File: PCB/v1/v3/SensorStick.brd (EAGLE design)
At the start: 58.4 x 38.1 mm, 57 parts, among them U1 TPD4F003DQDR, Y1 ECS-TXO-3225MV-400-TR

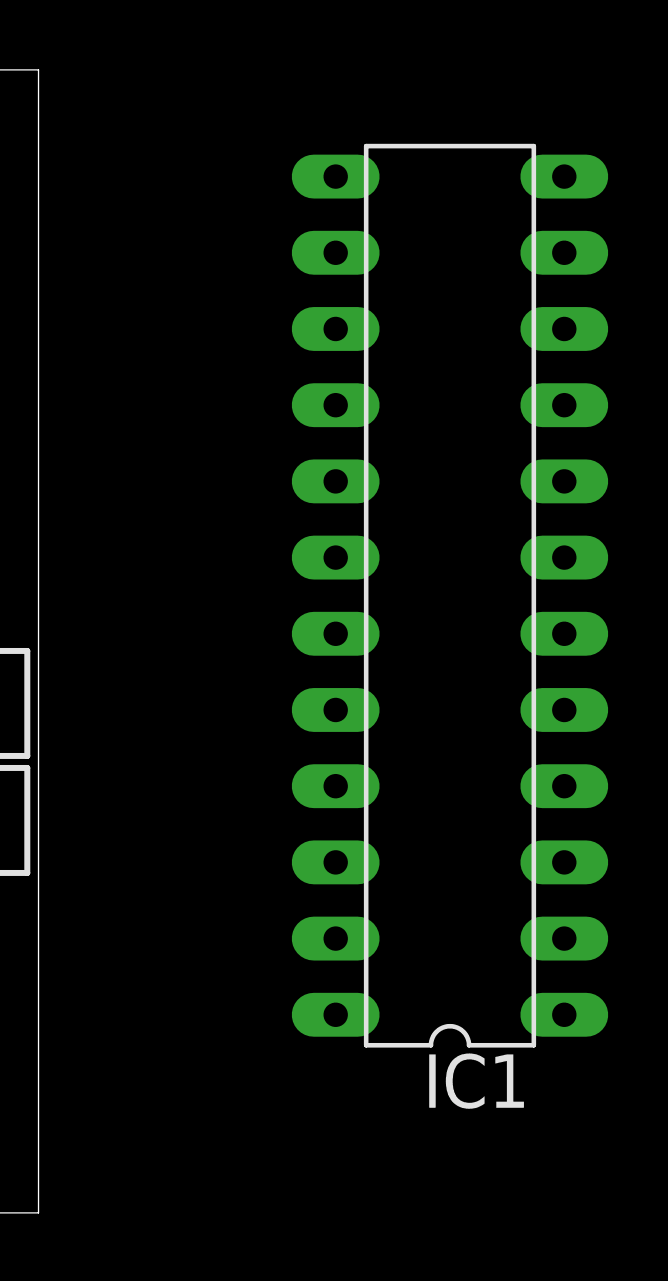
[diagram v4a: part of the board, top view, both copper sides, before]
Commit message: Jesus - Removed DIL24 IC connector
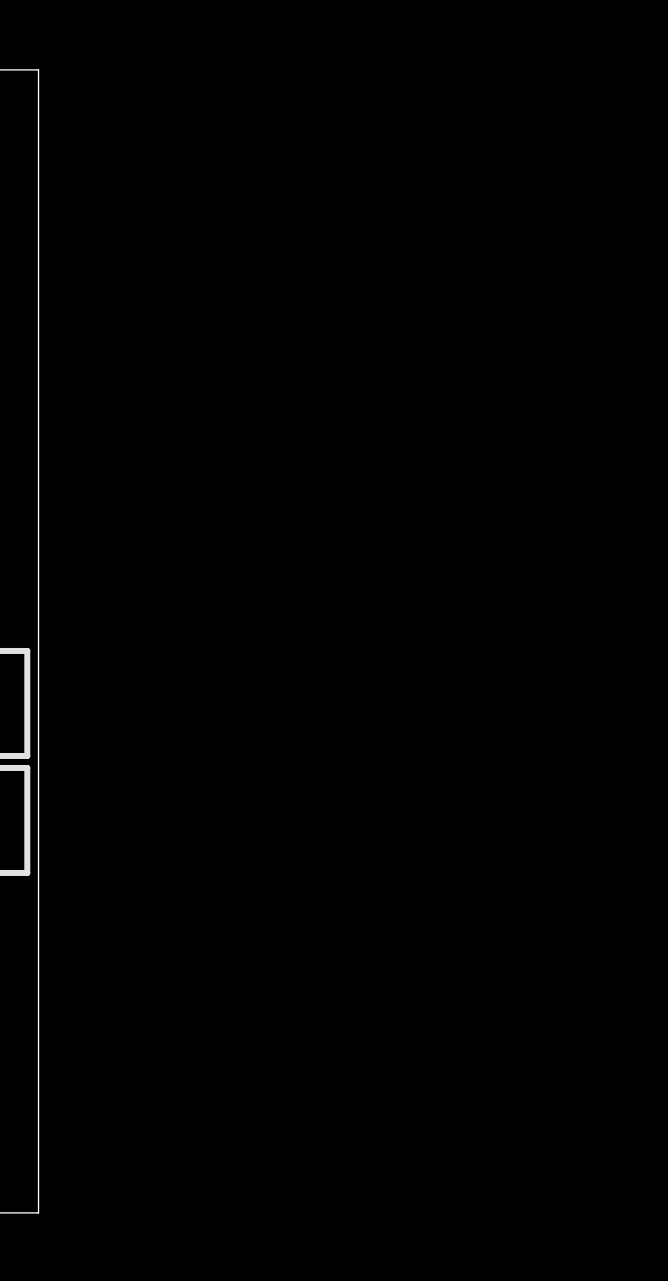
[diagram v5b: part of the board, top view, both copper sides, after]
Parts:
- removed IC1: (no value), ic-package:DIL24-3
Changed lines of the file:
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@@
 <attribute name="VALUE" x="48.387" y="30.226" size="1.27" layer="27" ratio="10" rot="R90"/>
-</element>
-<element name="IC1" library="ic-package" library_urn="urn:adsk.eagle:library:239" package="DIL24-3" package3d_urn="urn:adsk.eagle:package:3299/3" value="" x="72.136" y="20.574" smashed="yes" rot="R90">
-<attribute name="NAME" x="74.803" y="5.2832" size="1.778" layer="25" ratio="10" rot="R180"/>
-<attribute name="POPULARITY" value="0" x="72.136" y="20.574" size="1.778" layer="27" rot="R90" display="off"/>
-<attribute name="VALUE" x="73.025" y="7.112" size="1.778" layer="27" ratio="10" rot="R90"/>
 </element>
 <element name="JP1" library="pinhead" library_urn="urn:adsk.eagle:library:325" package="2X03" package3d_urn="urn:adsk.eagle:package:22462/2" value="" x="33.782" y="3.81" smashed="yes">

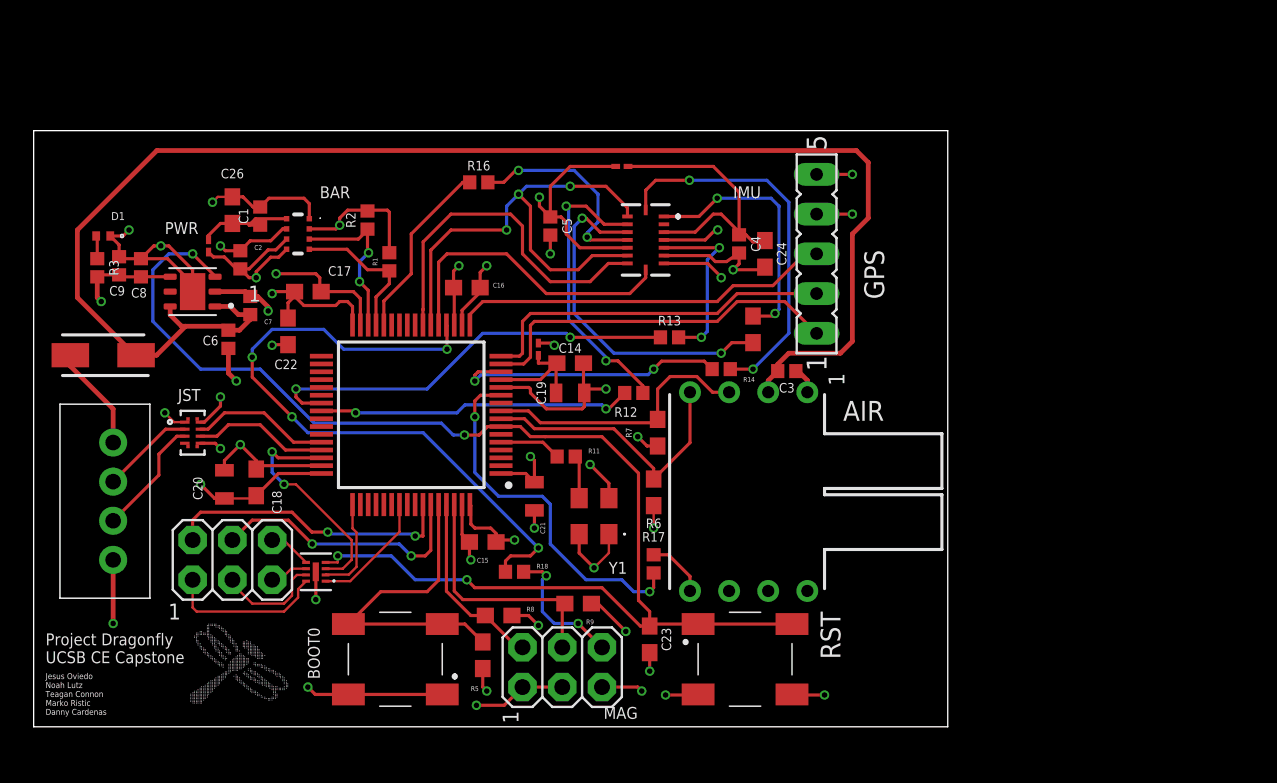
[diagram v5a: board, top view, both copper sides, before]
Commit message: Jesus - Rearranged to fit DIL24 socket for Mag breakout
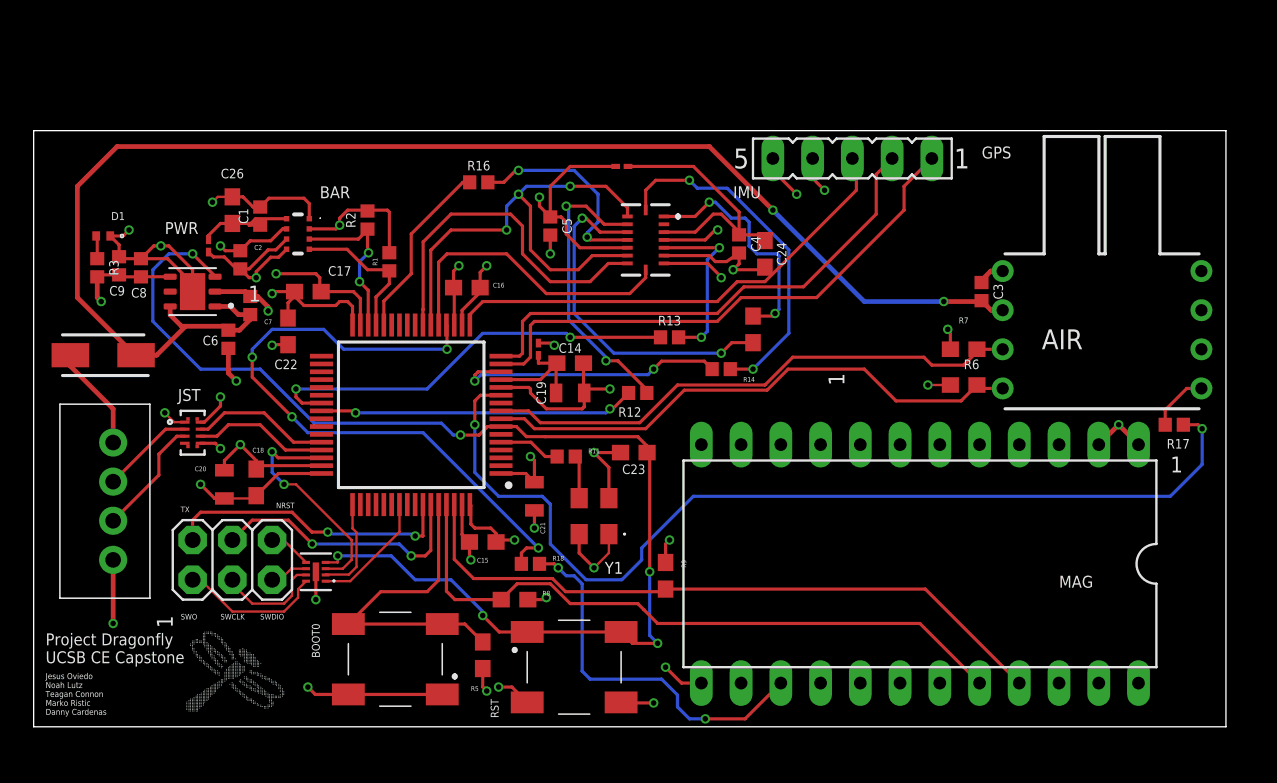
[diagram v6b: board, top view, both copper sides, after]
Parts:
- removed JP1: (no value), pinhead:2X03
- added IC2: (no value), ic-package:DIL24-6
- moved R17 34.4 mm to (72.9, 19.3), turned to 180 degrees
- moved AIRSPEED 26.1 mm to (70.2, 30.2), turned to 270 degrees
- moved R6 21.0 mm to (59.4, 21.8), turned to 180 degrees
- moved R7 20.3 mm to (59.4, 24.1), turned to 0 degrees
- moved C3 13.4 mm to (60.6, 27.8), turned to 270 degrees
- moved C23 12.0 mm to (38.4, 17.5), turned to 180 degrees
- moved S2 10.9 mm to (34.5, 3.81)
- moved SV1 6.51 mm to (52.3, 36.3), turned to 180 degrees
- moved R9 5.86 mm to (40.4, 9.65), turned to 270 degrees
- moved R8 1.44 mm to (30.7, 8.13)
- moved R18 1.14 mm to (31.8, 10.4)
- moved R12 0.25 mm to (38.6, 21.3)
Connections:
- net 3V3: now also IC2.1, IC2.2; no longer JP1.1, JP1.3
- net EXTI4: now also IC2.15; no longer JP1.6
- net GND: now also IC2.13; no longer JP1.5
- net I2C1_SCL: now also IC2.20; no longer JP1.2
- net I2C1_SDA: now also IC2.21; no longer JP1.4
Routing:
- net GPIO_EXTI3: track 23.5 -> 64.3 mm
- net I2C1_SCL: track 11.9 -> 42.9 mm
- net I2C1_SDA: track 15.8 -> 43.0 mm
- net I2C3_SDA: track 17.7 -> 34.9 mm
- net I2C3_SCL: track 18.3 -> 35.2 mm
- net EXTI4: track 8.71 -> 24.2 mm
- net GPIO_EXTI1: track 23.9 -> 35.1 mm
- net USART2_TX: track 23.0 -> 32.9 mm
- net USART2_RX: track 24.4 -> 30.8 mm
- net NRST: track 86.1 -> 80.6 mm, vias 4 -> 6
- net 5V: track 94.9 -> 90.0 mm, vias 0 -> 2
- net 3V3: track 103.2 -> 98.8 mm
- net EXTI0: track 24.3 -> 22.5 mm
- net GND: track 114.2 -> 115.9 mm, vias 28 -> 27
- net GPIO_EXTI4: track 42.8 -> 41.6 mm
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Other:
- board size 58.4 x 38.1 mm -> 76.2 x 38.1 mm
- board text added: "NRST"
- board text added: "SWCLK"
- board text added: "SWDIO"
- board text added: "SWO"
- board text added: "TX"
